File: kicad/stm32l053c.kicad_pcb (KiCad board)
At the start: 2 copper layers, 52 x 35 mm, 43 parts, among them P1 SWD, P2 PWR, Q1 BC807, Q2 BC817, SW1 SW_PUSH, SW2 SW_PUSH, SW3 SW_PUSH, SW4 SW_SPDT, U1 STM32L053C8_LQFP48, U2 TLV61225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

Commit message: Bottom initial routing
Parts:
- C4: moved to F.Cu
- moved R2 13.2 mm to (135.6, 87.3), turned to 180 degrees
- moved SW4 5.65 mm to (130.4, 87.0)
- moved C5 3.26 mm to (121.8, 99.8)
- moved C11 2.50 mm to (164.0, 100.6)
- moved P2 2.36 mm to (121.2, 91.8)
- moved R5 1.50 mm to (164.0, 102.6)
- moved D1 1.25 mm to (125.0, 100.8)
- moved C4 1.05 mm to (151.8, 89.1)
- moved R3 0.79 mm to (121.8, 101.8)
- moved Q2 0.61 mm to (134.0, 90.1)
- moved R7 0.51 mm to (133.3, 94.6)
- moved D2 0.40 mm to (146.8, 101.6)
- turned D3 to 90 degrees
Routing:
- net VDD: track 8.72 -> 150.8 mm, vias 0 -> 4
- net Earth: track 12.5 -> 77.0 mm, vias 0 -> 2
- net /WAKEUP_PIN1: track 8.80 -> 54.3 mm
- net /BUTTON0: track 0.00 -> 41.0 mm
- net /BUTTON2: track 0.00 -> 36.3 mm
- net NRST: track 0.00 -> 21.5 mm, vias 0 -> 1
- net /BUTTON1: track 0.00 -> 20.0 mm
- net +BATT: track 0.00 -> 6.47 mm
- net Net-(R3-Pad2): track 0.00 -> 6.21 mm, vias 0 -> 1
- net Net-(R5-Pad2): track 0.00 -> 5.62 mm, vias 0 -> 1
- net Net-(R4-Pad2): track 0.00 -> 5.37 mm, vias 0 -> 1
- net Net-(L1-Pad2): track 0.00 -> 4.39 mm
- net Net-(C8-Pad1): track 0.00 -> 3.26 mm
- net Net-(R2-Pad1): track 5.23 -> 8.41 mm
- net /VLCD: track 2.30 -> 3.82 mm, vias 0 -> 1
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- added copper zone on B.Cu, net Earth

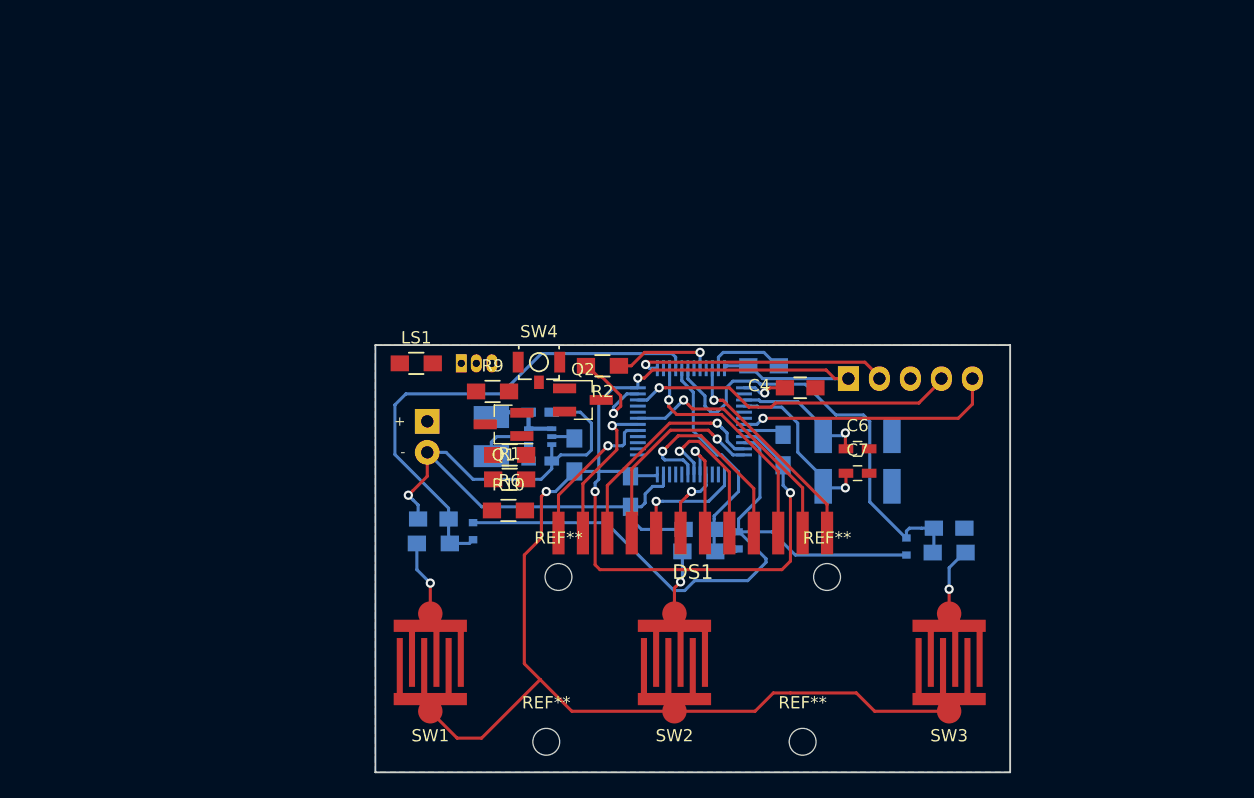
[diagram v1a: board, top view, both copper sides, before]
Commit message: Moved the MCU to the top of the board
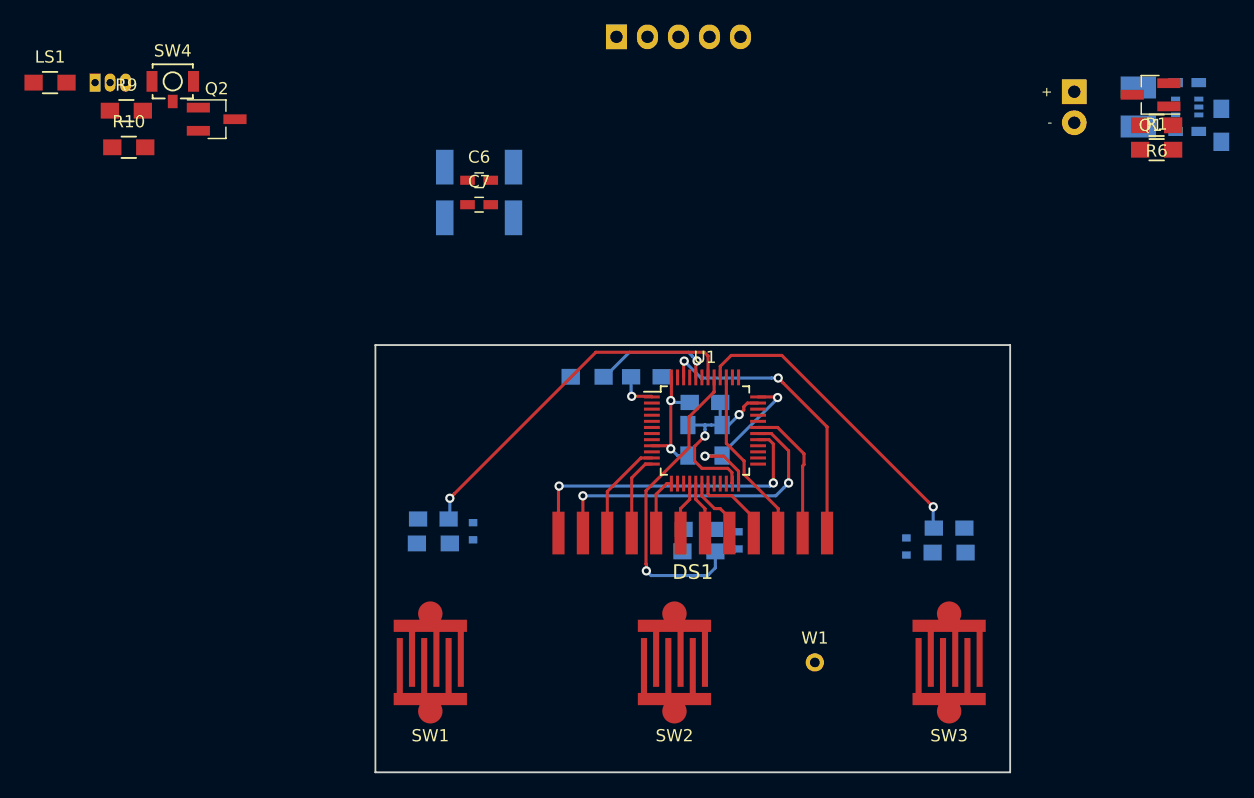
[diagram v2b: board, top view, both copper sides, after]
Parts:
- removed REF** (x4): MountingHole_2.2mm_M2, Mounting_Holes:MountingHole_2.2mm_M2
- removed REF**: TheApiLogoTiny, theapi:TheApiLogoTiny
- added W1: TEST_1P, Measurement_Points:Measurement_Point_Round-TH_Small, F.Cu at (153.0, 111.6)
- C4, R2: moved to B.Cu
- U1: moved to F.Cu
- moved C8 59.5 mm to (183.5, 68.1)
- moved C9 59.5 mm to (183.5, 64.1)
- moved L1 59.5 mm to (179.5, 66.1)
- moved P2 59.5 mm to (174.2, 64.8)
- moved Q1 59.5 mm to (180.5, 65.1)
- moved R1 59.5 mm to (181.0, 69.6)
- moved R6 59.5 mm to (181.0, 67.6)
- moved R7 59.5 mm to (186.3, 67.6)
- moved U2 59.5 mm to (183.5, 66.1)
- moved R10 43.0 mm to (96.8, 69.4)
- moved C6 38.0 mm to (125.5, 72.1)
- moved C7 38.0 mm to (125.5, 74.1)
- moved Y1 38.0 mm to (125.5, 73.1)
- moved LS1 37.8 mm to (90.3, 64.1)
- moved Q2 37.8 mm to (104.0, 67.1)
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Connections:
- C11 pad 1: /BUTTON2 -> /BUTTON0
- C5 pad 1: /BUTTON0 -> /BUTTON2
- R3 pad 1: /BUTTON0 -> /BUTTON2
- R5 pad 1: /BUTTON2 -> /BUTTON0
- U1 pad 15: (no net) -> Net-(U1-Pad15)
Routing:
- net VDD: track 150.8 -> 24.7 mm
- net Earth: track 77.0 -> 16.2 mm
- net /WAKEUP_PIN1: track 54.3 -> 0.00 mm
- net SWDIO: track 27.0 -> 0.00 mm, vias 1 -> 0
- net NRST: track 21.5 -> 0.00 mm, vias 1 -> 0
- net SWCLK: track 21.5 -> 0.00 mm, vias 1 -> 0
- net /BUTTON0: track 41.0 -> 25.6 mm, vias 0 -> 1
- net /OSC32_OUT: track 14.1 -> 0.00 mm, vias 1 -> 0
- net /LCD_COM1: track 12.3 -> 26.1 mm, vias 1 -> 2
- net /LCD_COM0: track 12.3 -> 26.1 mm, vias 1 -> 2
- net /OSC32_IN: track 11.3 -> 0.00 mm, vias 1 -> 0
- net /LCD_SEG6: track 17.1 -> 6.67 mm, vias 1 -> 0
- net /LCD_SEG0: track 18.5 -> 8.19 mm, vias 1 -> 0
- net /LCD_SEG1: track 16.6 -> 6.64 mm, vias 1 -> 0
- net /LCD_COM2: track 20.8 -> 11.2 mm, vias 1 -> 0
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- removed copper zone on B.Cu, net Earth

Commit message: Moved the buzzer pin to a more convenient location
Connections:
- U1 pad 14: (no net) -> Net-(U1-Pad14)
- U1 pad 2: (no net) -> Net-(U1-Pad2)
- U1 pad 20: (no net) -> Net-(U1-Pad20)
- U1 pad 21: (no net) -> Net-(U1-Pad21)
- U1 pad 22: /BUZZER -> Net-(U1-Pad22)
- U1 pad 26: (no net) -> Net-(U1-Pad26)
- U1 pad 27: (no net) -> Net-(U1-Pad27)
- U1 pad 28: (no net) -> Net-(U1-Pad28)
- U1 pad 32: (no net) -> Net-(U1-Pad32)
- U1 pad 33: (no net) -> Net-(U1-Pad33)
- U1 pad 38: (no net) -> /BUZZER
- U1 pad 43: (no net) -> Net-(U1-Pad43)
- U1 pad 45: (no net) -> Net-(U1-Pad45)
- U1 pad 5: (no net) -> Net-(U1-Pad5)
- U1 pad 6: (no net) -> Net-(U1-Pad6)
- Y1 pad 2: (no net) -> Net-(Y1-Pad2)
- Y1 pad 3: (no net) -> Net-(Y1-Pad3)
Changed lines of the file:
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@@
   (general
     (links 113)
-    (no_connects 82)
-    (area 87.167429 58.320999 189.529 135.515001)
+    (no_connects 81)
+    (area 116.924999 85.524999 169.075001 120.675001)
     (thickness 1.6)
     (drawings 20)
@@
     (zones 0)
     (modules 39)
-    (nets 42)
+    (nets 58)
   )
   (page A4)
@@
   (net 40 "Net-(R10-Pad2)")
   (net 41 "Net-(U1-Pad15)")
+  (net 42 "Net-(U1-Pad2)")
+  (net 43 "Net-(U1-Pad5)")
+  (net 44 "Net-(U1-Pad6)")
+  (net 45 "Net-(U1-Pad14)")
+  (net 46 "Net-(U1-Pad20)")
+  (net 47 "Net-(U1-Pad21)")
+  (net 48 "Net-(U1-Pad22)")
+  (net 49 "Net-(U1-Pad26)")
+  (net 50 "Net-(U1-Pad27)")
+  (net 51 "Net-(U1-Pad28)")
+  (net 52 "Net-(U1-Pad32)")
+  (net 53 "Net-(U1-Pad33)")
+  (net 54 "Net-(U1-Pad43)")
+  (net 55 "Net-(U1-Pad45)")
+  (net 56 "Net-(Y1-Pad2)")
+  (net 57 "Net-(Y1-Pad3)")
   (net_class Default "This is the default net class."
     (clearance 0.2032)
@@
     (add_net "Net-(R5-Pad2)")
     (add_net "Net-(R9-Pad2)")
+    (add_net "Net-(U1-Pad14)")
     (add_net "Net-(U1-Pad15)")
+    (add_net "Net-(U1-Pad2)")
+    (add_net "Net-(U1-Pad20)")
+    (add_net "Net-(U1-Pad21)")
+    (add_net "Net-(U1-Pad22)")
+    (add_net "Net-(U1-Pad26)")
+    (add_net "Net-(U1-Pad27)")
+    (add_net "Net-(U1-Pad28)")
+    (add_net "Net-(U1-Pad32)")
+    (add_net "Net-(U1-Pad33)")
+    (add_net "Net-(U1-Pad43)")
+    (add_net "Net-(U1-Pad45)")
+    (add_net "Net-(U1-Pad5)")
+    (add_net "Net-(U1-Pad6)")
+    (add_net "Net-(Y1-Pad2)")
+    (add_net "Net-(Y1-Pad3)")
     (add_net SWCLK)
     (add_net SWDIO)
@@
     (pad 1 smd rect (at -4.35 -2.75) (size 1.3 0.25) (layers F.Cu F.Paste F.Mask)
       (net 6 /VLCD))
-    (pad 2 smd rect (at -4.35 -2.25) (size 1.3 0.25) (layers F.Cu F.Paste F.Mask))
+    (pad 2 smd rect (at -4.35 -2.25) (size 1.3 0.25) (layers F.Cu F.Paste F.Mask)
+      (net 42 "Net-(U1-Pad2)"))
     (pad 3 smd rect (at -4.35 -1.75) (size 1.3 0.25) (layers F.Cu F.Paste F.Mask)
       (net 8 /OSC32_IN))
     (pad 4 smd rect (at -4.35 -1.25) (size 1.3 0.25) (layers F.Cu F.Paste F.Mask)
       (net 9 /OSC32_OUT))
-    (pad 5 smd rect (at -4.35 -0.75) (size 1.3 0.25) (layers F.Cu F.Paste F.Mask))
-    (pad 6 smd rect (at -4.35 -0.25) (size 1.3 0.25) (layers F.Cu F.Paste F.Mask))
+    (pad 5 smd rect (at -4.35 -0.75) (size 1.3 0.25) (layers F.Cu F.Paste F.Mask)
+      (net 43 "Net-(U1-Pad5)"))
+    (pad 6 smd rect (at -4.35 -0.25) (size 1.3 0.25) (layers F.Cu F.Paste F.Mask)
+      (net 44 "Net-(U1-Pad6)"))
     (pad 7 smd rect (at -4.35 0.25) (size 1.3 0.25) (layers F.Cu F.Paste F.Mask)
       (net 5 NRST))
@@
     (pad 13 smd rect (at -2.75 4.35 90) (size 1.3 0.25) (layers F.Cu F.Paste F.Mask)
       (net 18 /LCD_SEG2))
-    (pad 14 smd rect (at -2.25 4.35 90) (size 1.3 0.25) (layers F.Cu F.Paste F.Mask))
+    (pad 14 smd rect (at -2.25 4.35 90) (size 1.3 0.25) (layers F.Cu F.Paste F.Mask)
+      (net 45 "Net-(U1-Pad14)"))
     (pad 15 smd rect (at -1.75 4.35 90) (size 1.3 0.25) (layers F.Cu F.Paste F.Mask)
       (net 41 "Net-(U1-Pad15)"))
@@
     (pad 19 smd rect (at 0.25 4.35 90) (size 1.3 0.25) (layers F.Cu F.Paste F.Mask)
       (net 22 /LCD_SEG6))
-    (pad 20 smd rect (at 0.75 4.35 90) (size 1.3 0.25) (layers F.Cu F.Paste F.Mask))
-    (pad 21 smd rect (at 1.25 4.35 90) (size 1.3 0.25) (layers F.Cu F.Paste F.Mask))
+    (pad 20 smd rect (at 0.75 4.35 90) (size 1.3 0.25) (layers F.Cu F.Paste F.Mask)
+      (net 46 "Net-(U1-Pad20)"))
+    (pad 21 smd rect (at 1.25 4.35 90) (size 1.3 0.25) (layers F.Cu F.Paste F.Mask)
+      (net 47 "Net-(U1-Pad21)"))
     (pad 22 smd rect (at 1.75 4.35 90) (size 1.3 0.25) (layers F.Cu F.Paste F.Mask)
-      (net 33 /BUZZER))
+      (net 48 "Net-(U1-Pad22)"))
     (pad 23 smd rect (at 2.25 4.35 90) (size 1.3 0.25) (layers F.Cu F.Paste F.Mask)
       (net 2 Earth))
@@
     (pad 25 smd rect (at 4.35 2.75) (size 1.3 0.25) (layers F.Cu F.Paste F.Mask)
       (net 34 /MELODY))
-    (pad 26 smd rect (at 4.35 2.25) (size 1.3 0.25) (layers F.Cu F.Paste F.Mask))
-    (pad 27 smd rect (at 4.35 1.75) (size 1.3 0.25) (layers F.Cu F.Paste F.Mask))
-    (pad 28 smd rect (at 4.35 1.25) (size 1.3 0.25) (layers F.Cu F.Paste F.Mask))
+    (pad 26 smd rect (at 4.35 2.25) (size 1.3 0.25) (layers F.Cu F.Paste F.Mask)
+      (net 49 "Net-(U1-Pad26)"))
+    (pad 27 smd rect (at 4.35 1.75) (size 1.3 0.25) (layers F.Cu F.Paste F.Mask)
+      (net 50 "Net-(U1-Pad27)"))
+    (pad 28 smd rect (at 4.35 1.25) (size 1.3 0.25) (layers F.Cu F.Paste F.Mask)
+      (net 51 "Net-(U1-Pad28)"))
     (pad 29 smd rect (at 4.35 0.75) (size 1.3 0.25) (layers F.Cu F.Paste F.Mask)
       (net 14 /LCD_COM0))
@@
     (pad 31 smd rect (at 4.35 -0.25) (size 1.3 0.25) (layers F.Cu F.Paste F.Mask)
       (net 24 /LCD_COM2))
-    (pad 32 smd rect (at 4.35 -0.75) (size 1.3 0.25) (layers F.Cu F.Paste F.Mask))
-    (pad 33 smd rect (at 4.35 -1.25) (size 1.3 0.25) (layers F.Cu F.Paste F.Mask))
+    (pad 32 smd rect (at 4.35 -0.75) (size 1.3 0.25) (layers F.Cu F.Paste F.Mask)
+      (net 52 "Net-(U1-Pad32)"))
+    (pad 33 smd rect (at 4.35 -1.25) (size 1.3 0.25) (layers F.Cu F.Paste F.Mask)
+      (net 53 "Net-(U1-Pad33)"))
     (pad 34 smd rect (at 4.35 -1.75) (size 1.3 0.25) (layers F.Cu F.Paste F.Mask)
       (net 4 SWDIO))
@@
     (pad 37 smd rect (at 2.75 -4.35 90) (size 1.3 0.25) (layers F.Cu F.Paste F.Mask)
       (net 3 SWCLK))
-    (pad 38 smd rect (at 2.25 -4.35 90) (size 1.3 0.25) (layers F.Cu F.Paste F.Mask))
+    (pad 38 smd rect (at 2.25 -4.35 90) (size 1.3 0.25) (layers F.Cu F.Paste F.Mask)
+      (net 33 /BUZZER))
     (pad 39 smd rect (at 1.75 -4.35 90) (size 1.3 0.25) (layers F.Cu F.Paste F.Mask)
       (net 23 /LCD_SEG7))
@@
     (pad 42 smd rect (at 0.25 -4.35 90) (size 1.3 0.25) (layers F.Cu F.Paste F.Mask)
       (net 13 /BUTTON2))
-    (pad 43 smd rect (at -0.25 -4.35 90) (size 1.3 0.25) (layers F.Cu F.Paste F.Mask))
+    (pad 43 smd rect (at -0.25 -4.35 90) (size 1.3 0.25) (layers F.Cu F.Paste F.Mask)
+      (net 54 "Net-(U1-Pad43)"))
     (pad 44 smd rect (at -0.75 -4.35 90) (size 1.3 0.25) (layers F.Cu F.Paste F.Mask)
       (net 27 "Net-(R2-Pad1)"))
-    (pad 45 smd rect (at -1.25 -4.35 90) (size 1.3 0.25) (layers F.Cu F.Paste F.Mask))
+    (pad 45 smd rect (at -1.25 -4.35 90) (size 1.3 0.25) (layers F.Cu F.Paste F.Mask)
+      (net 55 "Net-(U1-Pad45)"))
     (pad 46 smd rect (at -1.75 -4.35 90) (size 1.3 0.25) (layers F.Cu F.Paste F.Mask)
       (net 25 /LCD_COM3))
@@
     (pad 1 smd rect (at -2.815 -2.075) (size 1.43 2.85) (layers B.Cu B.Mask)
       (net 8 /OSC32_IN))
-    (pad 2 smd rect (at 2.815 -2.075) (size 1.43 2.85) (layers B.Cu B.Mask))
-    (pad 3 smd rect (at 2.815 2.075) (size 1.43 2.85) (layers B.Cu B.Mask))
+    (pad 2 smd rect (at 2.815 -2.075) (size 1.43 2.85) (layers B.Cu B.Mask)
+      (net 56 "Net-(Y1-Pad2)"))
+    (pad 3 smd rect (at 2.815 2.075) (size 1.43 2.85) (layers B.Cu B.Mask)
+      (net 57 "Net-(Y1-Pad3)"))
     (pad 4 smd rect (at -2.815 2.075) (size 1.43 2.85) (layers B.Cu B.Mask)
       (net 9 /OSC32_OUT))

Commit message: Layout
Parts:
- added REF**: MountingHole_2.2mm_M2, Mounting_Holes:MountingHole_2.2mm_M2, F.Cu at (131.0, 118.1)
- added REF**: MountingHole_2.2mm_M2, Mounting_Holes:MountingHole_2.2mm_M2, F.Cu at (152.0, 118.1)
- added REF**: MountingHole_2.2mm_M2, Mounting_Holes:MountingHole_2.2mm_M2, F.Cu at (154.0, 104.6)
- added REF**: MountingHole_2.2mm_M2, Mounting_Holes:MountingHole_2.2mm_M2, F.Cu at (132.0, 104.6)
- LS1, Q1, R1: moved to B.Cu
- SW4: footprint Buttons_Switches_SMD:SW_SPST_B3U-1100P -> Pin_Headers:Pin_Header_Straight_1x03_Pitch2.54mm
- moved LS1 81.1 mm to (167.5, 89.1), turned to 270 degrees
- moved R9 65.8 mm to (157.2, 91.8)
- moved R10 65.2 mm to (157.2, 93.8)
- moved SW4 64.1 mm to (160.0, 87.6), turned to 90 degrees
- moved Q2 63.9 mm to (163.0, 91.6), turned to 270 degrees
- moved U3 62.8 mm to (154.8, 87.6), turned to 0 degrees
- moved R7 43.5 mm to (156.0, 98.8), turned to 0 degrees
- moved C9 39.6 mm to (159.9, 96.0), turned to 270 degrees
- moved U2 39.3 mm to (157.9, 96.0), turned to 180 degrees
- moved C8 39.2 mm to (155.9, 96.0), turned to 270 degrees
- moved R6 36.9 mm to (157.2, 95.8), turned to 0 degrees
- moved D3 36.0 mm to (124.5, 100.8), turned to 270 degrees
- moved D1 35.7 mm to (160.7, 101.6), turned to 90 degrees
- moved R1 34.0 mm to (152.5, 88.1), turned to 270 degrees
- moved L1 33.7 mm to (157.9, 92.0), turned to 180 degrees
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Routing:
- net /WAKEUP_PIN1: track 0.00 -> 61.4 mm, vias 0 -> 1
- net Earth: track 16.2 -> 58.1 mm, vias 2 -> 5
- net SWCLK: track 0.00 -> 30.4 mm, vias 0 -> 1
- net SWDIO: track 0.00 -> 27.0 mm, vias 0 -> 2
- net VDD: track 24.7 -> 45.7 mm
- net NRST: track 0.00 -> 18.2 mm
- net Net-(U1-Pad15): track 0.00 -> 15.3 mm
- net /OSC32_IN: track 0.00 -> 11.9 mm, vias 0 -> 2
- net /MELODY: track 0.00 -> 10.4 mm, vias 0 -> 1
- net /OSC32_OUT: track 0.00 -> 9.87 mm, vias 0 -> 2
- net /BUZZER: track 0.00 -> 8.94 mm, vias 0 -> 1
- net /BUTTON2: track 29.7 -> 37.3 mm
- net +BATT: track 0.00 -> 7.04 mm
- net Net-(C8-Pad1): track 0.00 -> 5.69 mm
- net Net-(L1-Pad2): track 0.00 -> 3.71 mm
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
